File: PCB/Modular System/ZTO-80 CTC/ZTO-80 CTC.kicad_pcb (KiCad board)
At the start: 2 copper layers, 99.1 x 57.1 mm, 18 parts, among them J1 ZTO-80 Bus, J2 Conn_01x02, J3 Conn_01x08, SW1 SW_DIP_x06, U1 Z80CTC, U2 74HC688

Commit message: Edited power LED resistor value
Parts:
- R1: value 200 -> 220

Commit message: Updates to PDFs and the SBC
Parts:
- added JP6: Jumper_2_Open, Connector_PinHeader_2.54mm:PinHeader_1x02_P2.54mm_Vertical, F.Cu at (156.2, 99.1)
- moved J3 1.27 mm to (191.1, 66.7)
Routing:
- net /CLK: track 38.2 -> 59.1 mm
- net /ZT1: track 88.5 -> 91.3 mm
- net /CT0: track 54.0 -> 56.4 mm
- net /CT2: track 72.3 -> 71.2 mm
- net /ZT0: track 44.2 -> 43.6 mm
- net /CT3: track 51.8 -> 51.2 mm
- net /CT1: track 62.5 -> 62.0 mm
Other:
- board text added: "CLK"
- board text added: "ZTO-80 CTC"
- board text added: "v1.0"
- board text removed: "BACK"
- board text removed: "ZTO-80 CTC V1.0"

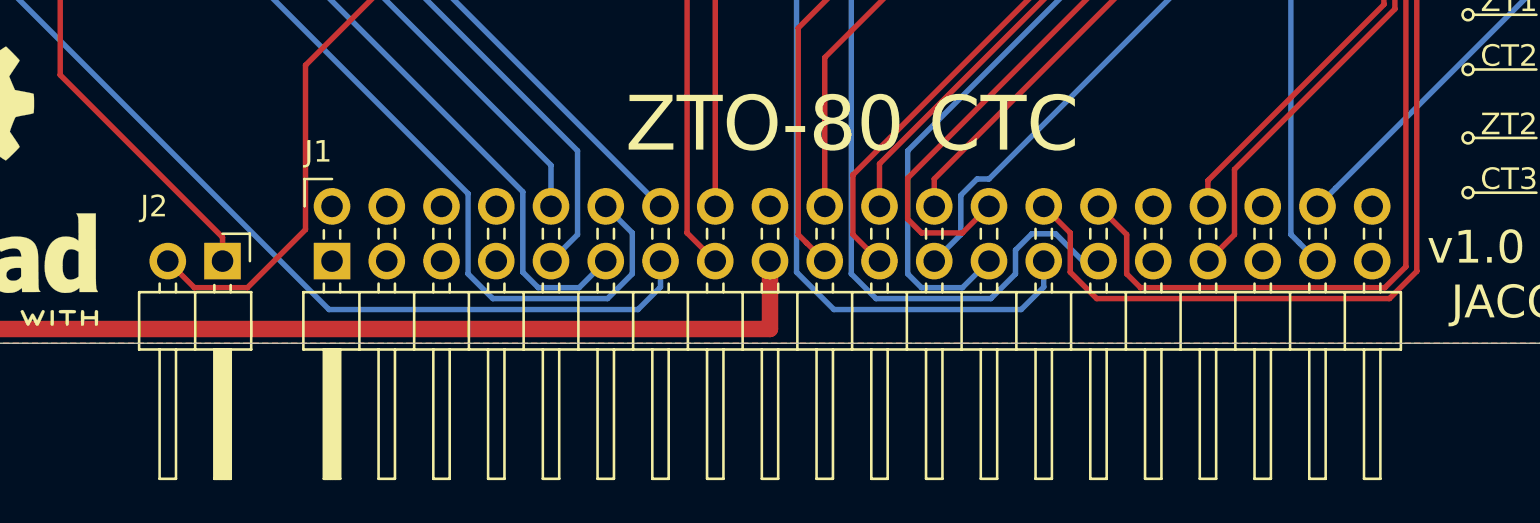
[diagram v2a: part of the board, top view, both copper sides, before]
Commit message: Changed bus orientation
This change is backwards-compatible with all previous ZTO-80 modules
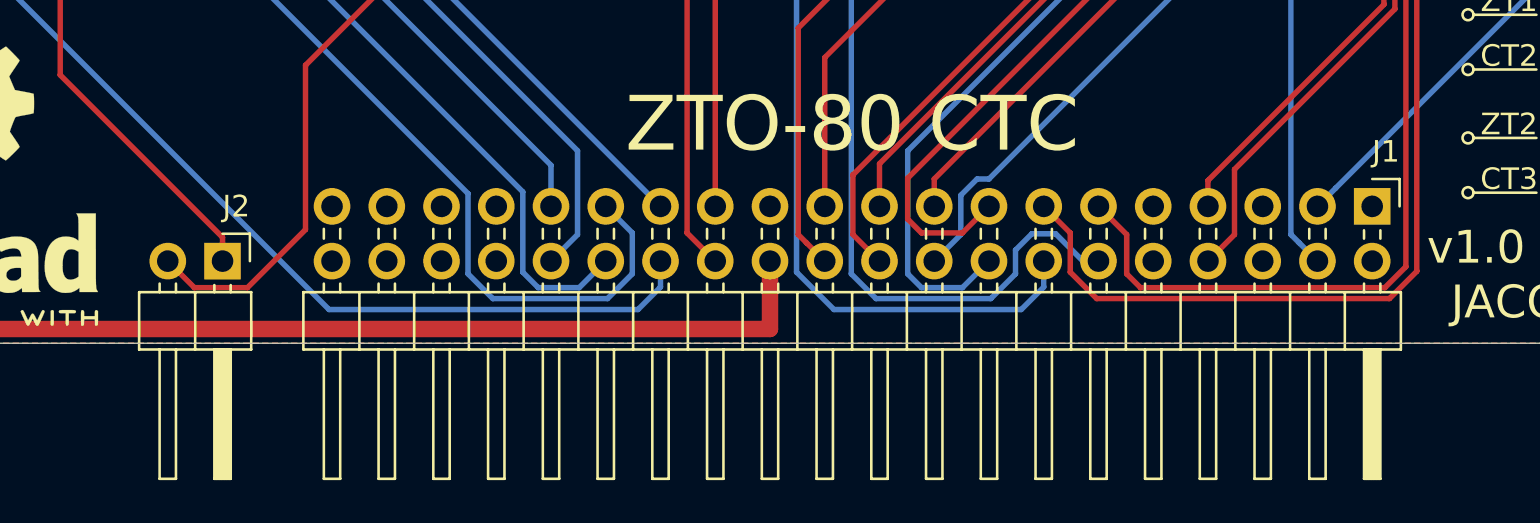
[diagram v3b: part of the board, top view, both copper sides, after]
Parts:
- J1: footprint ZTO-80_Header:PinHeader_2x20_P2.54mm_Horizontal -> Connector_PinHeader_2.54mm:PinHeader_2x20_P2.54mm_Horizontal
- moved J1 48.3 mm to (169.5, 113.7), turned to 270 degrees
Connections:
- J1 pad 1: /A15 -> /USR4
- J1 pad 10: /A6 -> /MREQ
- J1 pad 11: /A5 -> /INT
- J1 pad 12: /A4 -> /RST
- J1 pad 13: /A3 -> /M1
- J1 pad 14: /A2 -> /CLK
- J1 pad 15: /A1 -> /D0
- J1 pad 16: /A0 -> /D1
- J1 pad 17: VCC -> /D2
- J1 pad 18: GND -> /D3
- J1 pad 19: /D7 -> /D4
- J1 pad 2: /A14 -> /USR3
- J1 pad 20: /D6 -> /D5
- J1 pad 21: /D5 -> /D6
- J1 pad 22: /D4 -> /D7
- J1 pad 23: /D3 -> GND
- J1 pad 24: /D2 -> VCC
- J1 pad 25: /D1 -> /A0
- J1 pad 26: /D0 -> /A1
- J1 pad 27: /CLK -> /A2
- J1 pad 28: /M1 -> /A3
- J1 pad 29: /RST -> /A4
- J1 pad 3: /A13 -> /USR2
- J1 pad 30: /INT -> /A5
- J1 pad 31: /MREQ -> /A6
- J1 pad 32: /WR -> /A7
- J1 pad 33: /IORQ -> /A8
- J1 pad 34: /RD -> /A9
- J1 pad 35: /TXB -> /A10
- J1 pad 36: /RXB -> /A11
- J1 pad 37: /USR1 -> /A12
- J1 pad 38: /USR2 -> /A13
- J1 pad 39: /USR3 -> /A14
- J1 pad 4: /A12 -> /USR1
- J1 pad 40: /USR4 -> /A15
- J1 pad 5: /A11 -> /RXB
- J1 pad 6: /A10 -> /TXB
- J1 pad 7: /A9 -> /RD
- J1 pad 8: /A8 -> /IORQ
- J1 pad 9: /A7 -> /WR

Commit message: Added CERN license text to silkscreen
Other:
- board text added: "Licensed under CERN-OHL-S v2"
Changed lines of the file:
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@@
   (general
     (thickness 1.6)
-    (drawings 99)
+    (drawings 100)
     (tracks 301)
     (zones 0)
@@
     )
   )
+  (gr_text "Licensed under CERN-OHL-S v2" (at 109.22 118.745) (layer B.SilkS)
+    (effects (font (size 1 1) (thickness 0.15)) (justify mirror))
+  )
   (gr_text v1.0 (at 172.085 115.57) (layer F.SilkS)

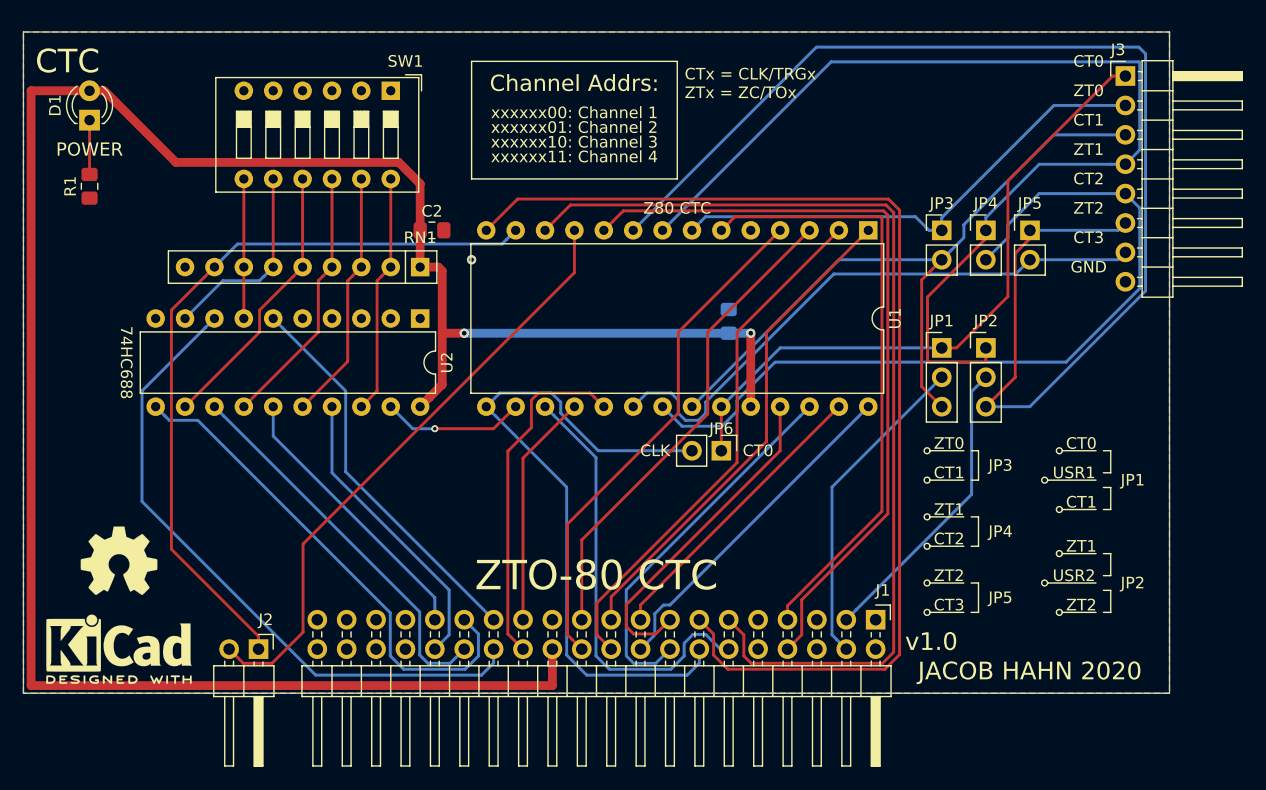
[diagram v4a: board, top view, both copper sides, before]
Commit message: Finished CTC
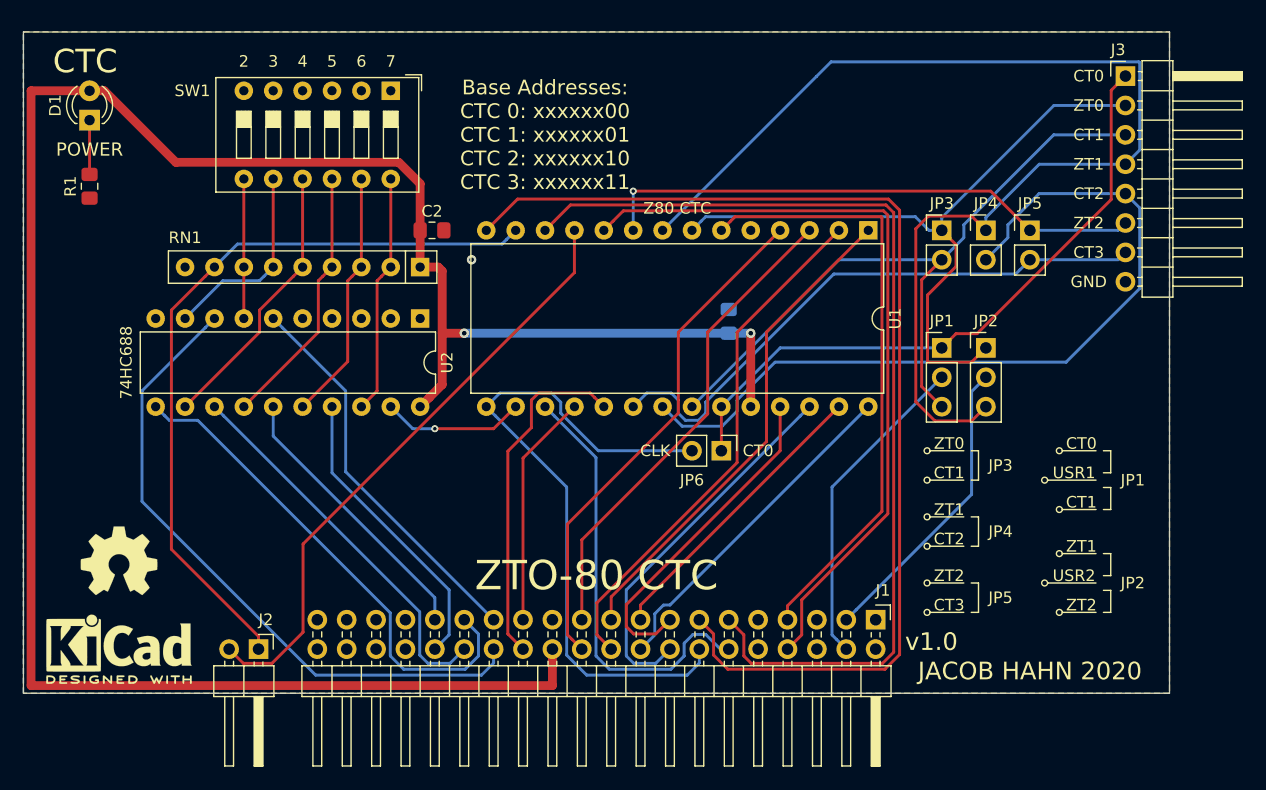
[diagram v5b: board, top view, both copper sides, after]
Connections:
- JP2 pad 1: /ZT1 -> /ZT0
- JP2 pad 3: /ZT2 -> /ZT1
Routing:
- net /ZT2: track 114.9 -> 47.6 mm, vias 0 -> 1
- net /ZT0: track 43.6 -> 62.0 mm
- net /ZT1: track 91.3 -> 100.9 mm
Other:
- board text added: "2"
- board text added: "3"
- board text added: "4"
- board text added: "5"
- board text added: "6"
- board text added: "7"
- board text added: "Base Addresses: CTC 0: xxxxxx00 CTC 1: xxxxxx01 CTC 2: xxxxxx10 CTC 3: xxxxxx11"
- board text removed: "CTx = CLK/TRGx ZTx = ZC/TOx"
- board text removed: "Channel Addrs:"
- board text removed: "xxxxxx00: Channel 1"
- board text removed: "xxxxxx01: Channel 2"
- board text removed: "xxxxxx10: Channel 3"
- board text removed: "xxxxxx11: Channel 4"
